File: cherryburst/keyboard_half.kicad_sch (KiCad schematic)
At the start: 51 parts, among them J201 USB_C_Receptacle_USB2.0, J202 tag-connect-swd, J203 LCD, U201 nRF52833-QDxx, U202 USBLC6-2SC6, U203 TPS70630DBVR, U204 MCP73832-2-OT, Y201 32 MHz

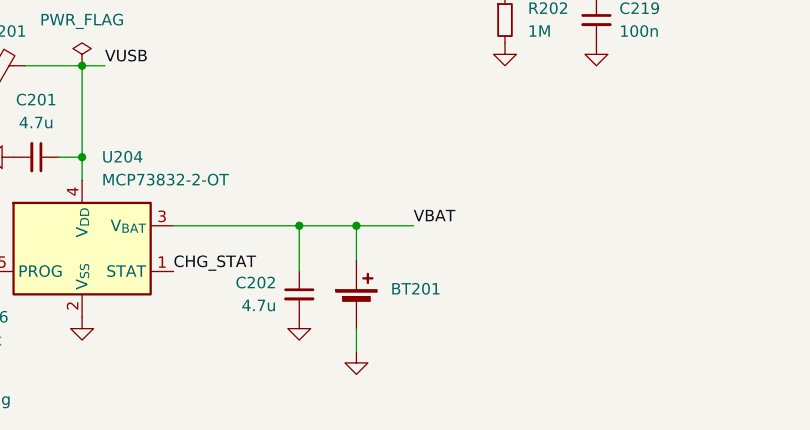
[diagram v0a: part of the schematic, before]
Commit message: Some small fixes for battery connector
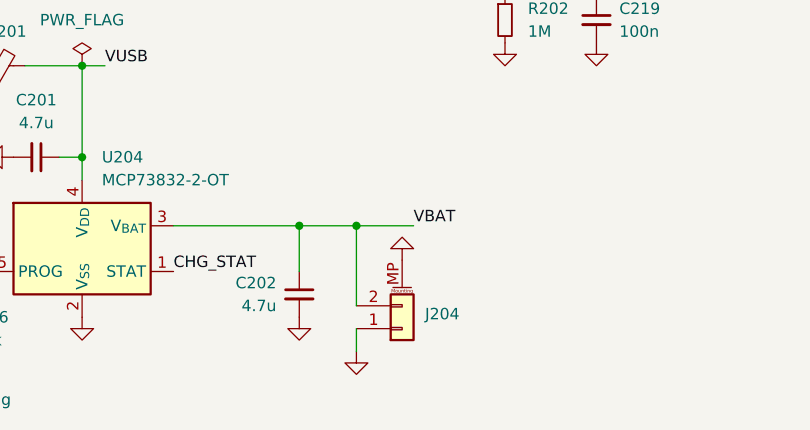
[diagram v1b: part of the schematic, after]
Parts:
- removed BT201: Battery_Cell, connectors:1x2_2.54mm, symbol Device:Battery_Cell
- added J204: Conn_01x02_MountingPin, Connector_JST:JST_SH_SM02B-SRSS-TB_1x02-1MP_P1.00mm_Horizontal, symbol Connector_Generic_MountingPin:Conn_01x02_MountingPin
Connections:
- net GND: now also J204.1 (Pin_1), J204.MP (MountPin)
- net VBAT: now also J204.2 (Pin_2)
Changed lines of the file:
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@@
     (stroke (width 0) (type default))
   )
-  (wire (pts (xy 151.13 172.72) (xy 151.13 176.53))
+  (wire (pts (xy 151.13 172.72) (xy 151.13 181.61))
     (stroke (width 0) (type default))
   )
@@
     (stroke (width 0) (type default))
   )
+  (wire (pts (xy 151.13 184.15) (xy 151.13 186.69))
+    (stroke (width 0) (type default))
+  )
   (wire (pts (xy 160.02 64.77) (xy 160.02 66.04))
     (stroke (width 0) (type default))
@@
     (stroke (width 0) (type default))
   )
-  (wire (pts (xy 151.13 184.15) (xy 151.13 186.69))
-    (stroke (width 0) (type default))
-  )
   (wire (pts (xy 161.29 19.05) (xy 165.1 19.05))
     (stroke (width 0) (type default))
@@
     )
   )
+  (symbol (lib_id "Connector_Generic_MountingPin:Conn_01x02_MountingPin") (at 156.21 184.15 0) (mirror x) (unit 1)
+    (in_bom yes) (on_board yes) (dnp no)
+    (property "Reference" "J204" (at 158.75 182.5244 0)
+      (effects (font (size 1.27 1.27)) (justify left))
+    )
+    (property "Value" "Conn_01x02_MountingPin" (at 158.75 181.2544 0)
+      (effects (font (size 1.27 1.27)) (justify left) hide)
+    )
+    (property "Footprint" "Connector_JST:JST_SH_SM02B-SRSS-TB_1x02-1MP_P1.00mm_Horizontal" (at 156.21 184.15 0)
+      (effects (font (size 1.27 1.27)) hide)
+    )
+    (property "Datasheet" "~" (at 156.21 184.15 0)
+      (effects (font (size 1.27 1.27)) hide)
+    )
+    (property "MFPN" "" (at 156.21 184.15 0)
+      (effects (font (size 1.27 1.27)) hide)
+    )
+    (property "Specification" "" (at 156.21 184.15 0)
+      (effects (font (size 1.27 1.27)) hide)
+    )
+    (property "LCSC" "" (at 156.21 184.15 0)
+      (effects (font (size 1.27 1.27)) hide)
+    )
+    (pin "1")
+    (pin "2")
+    (pin "MP")
+    (instances
+      (project "crkbd-shockburst"
+        (path "/76f7b6ad-1528-4ee8-9fc0-4578616aebf5/03cbda14-d368-4dde-b0d5-76768308216d"
+          (reference "J204") (unit 1)
+        )
+        (path "/76f7b6ad-1528-4ee8-9fc0-4578616aebf5/3b44a955-2a37-4d30-8a82-5f0155f54e66"
+          (reference "J504") (unit 1)
+        )
+      )
+    )
+  )
   (symbol (lib_id "power:GND") (at 69.85 125.73 0) (unit 1)
     (in_bom yes) (on_board yes) (dnp no) (fields_autoplaced)
@@
     )
   )
+  (symbol (lib_id "power:GND") (at 156.21 176.53 180) (unit 1)
+    (in_bom yes) (on_board yes) (dnp no) (fields_autoplaced)
+    (property "Reference" "#PWR0214" (at 156.21 170.18 0)
+      (effects (font (size 1.27 1.27)) hide)
+    )
+    (property "Value" "GND" (at 156.21 171.45 0)
+      (effects (font (size 1.27 1.27)) hide)
+    )
+    (property "Footprint" "" (at 156.21 176.53 0)
+      (effects (font (size 1.27 1.27)) hide)
+    )
+    (property "Datasheet" "" (at 156.21 176.53 0)
+      (effects (font (size 1.27 1.27)) hide)
+    )
+    (pin "1")
+    (instances
+      (project "crkbd-shockburst"
+        (path "/76f7b6ad-1528-4ee8-9fc0-4578616aebf5/03cbda14-d368-4dde-b0d5-76768308216d"
+          (reference "#PWR0214") (unit 1)
+        )
+        (path "/76f7b6ad-1528-4ee8-9fc0-4578616aebf5/3b44a955-2a37-4d30-8a82-5f0155f54e66"
+          (reference "#PWR0510") (unit 1)
+        )
+      )
+    )
+  )
   (symbol (lib_id "Device:L_Small") (at 167.64 19.05 90) (unit 1)
     (in_bom yes) (on_board yes) (dnp yes) (fields_autoplaced)
@@
         )
       )
-    )
-  )
-  (symbol (lib_id "Device:Battery_Cell") (at 151.13 181.61 0) (unit 1)
-    (in_bom yes) (on_board yes) (dnp no) (fields_autoplaced)
-    (property "Reference" "BT201" (at 154.94 179.7685 0)
-      (effects (font (size 1.27 1.27)) (justify left))
-    )
-    (property "Value" "Battery_Cell" (at 154.94 181.0385 0)
-      (effects (font (size 1.27 1.27)) (justify left) hide)
-    )
-    (property "Footprint" "connectors:1x2_2.54mm" (at 151.13 180.086 90)
-      (effects (font (size 1.27 1.27)) hide)
-    )
-    (property "Datasheet" "~" (at 151.13 180.086 90)
-      (effects (font (size 1.27 1.27)) hide)
-    )
-    (pin "1")
-    (pin "2")
-    (instances
-      (project "crkbd-shockburst"
-        (path "/76f7b6ad-1528-4ee8-9fc0-4578616aebf5/03cbda14-d368-4dde-b0d5-76768308216d"
-          (reference "BT201") (unit 1)
-        )
-        (path "/76f7b6ad-1528-4ee8-9fc0-4578616aebf5/3b44a955-2a37-4d30-8a82-5f0155f54e66"
-          (reference "BT501") (unit 1)
-        )
-      )
